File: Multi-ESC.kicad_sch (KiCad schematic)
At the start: 0 parts

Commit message: selected parts
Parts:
- added U3: LMR51450FN, Package_TO_SOT_SMD:SOT-23-6, symbol Multi-ESC:LMR51450FN
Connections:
- new net: U3.1 (SW), U3.2 (SW), U3.3 (SW)
- new net VIN: U3.10 (VIN), U3.11 (VIN), U3.12 (VIN)
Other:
- added sheet BLDC Driver (bldc_driver.kicad_sch)
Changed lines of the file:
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@@
 	(generator_version "10.0")
 	(paper "A4")
+	(symbol
+		(lib_id "Multi-ESC:LMR51450FN")
+		(at 88.9 55.88 0)
+		(unit 1)
+		(body_style 1)
+		(exclude_from_sim no)
+		(in_bom yes)
+		(on_board yes)
+		(in_pos_files yes)
+		(dnp no)
+		(fields_autoplaced yes)
+		(property "Reference" "U3"
+			(at 88.9 45.72 0)
+			(show_name no)
+			(do_not_autoplace no)
+			(effects
+				(font
+					(size 1.27 1.27)
+				)
+			)
+		)
+		(property "Value" "LMR51450FN"
+			(at 88.9 48.26 0)
+			(show_name no)
+			(do_not_autoplace no)
+			(effects
+				(font
+					(size 1.27 1.27)
+				)
+			)
+		)
+		(property "Footprint" "Package_TO_SOT_SMD:SOT-23-6"
+			(at 90.17 73.914 0)
+			(hide yes)
+			(show_name no)
+			(do_not_autoplace no)
+			(effects
+				(font
+					(size 1.27 1.27)
+				)
+				(justify left)
+			)
+		)
+		(property "Datasheet" "https://www.ti.com/lit/ds/symlink/lmr51450.pdf"
+			(at 90.17 76.454 0)
+			(hide yes)
+			(show_name no)
+			(do_not_autoplace no)
+			(effects
+				(font
+					(size 1.27 1.27)
+				)
+				(justify left)
+			)
+		)
+		(property "Description" "4.5-V to 36-V, 3-A synchronous buck converter with 40-µA IQ, SOT-23-6"
+			(at 88.9 55.88 0)
+			(hide yes)
+			(show_name no)
+			(do_not_autoplace no)
+			(effects
+				(font
+					(size 1.27 1.27)
+				)
+			)
+		)
+		(pin "12"
+		)
+		(pin "9"
+		)
+		(pin "8"
+		)
+		(pin "7"
+		)
+		(pin "1"
+		)
+		(pin "2"
+		)
+		(pin "6"
+		)
+		(pin "10"
+		)
+		(pin "11"
+		)
+		(pin "13"
+		)
+		(pin "3"
+		)
+		(pin "5"
+		)
+		(pin "4"
+		)
+		(instances
+			(project "Multi-ESC"
+				(path "/332a84c1-656a-45ff-900c-4414e0318fba"
+					(reference "U3")
+					(unit 1)
+				)
+			)
+		)
+	)
+	(sheet
+		(at 194.31 44.45)
+		(size 25.4 15.24)
+		(exclude_from_sim no)
+		(in_bom yes)
+		(on_board yes)
+		(dnp no)
+		(fields_autoplaced yes)
+		(stroke
+			(width 0.1524)
+			(type solid)
+		)
+		(fill
+			(color 0 0 0 0)
+		)
+		(property "Sheetname" "BLDC Driver"
+			(at 194.31 43.7384 0)
+			(show_name no)
+			(do_not_autoplace no)
+			(effects
+				(font
+					(size 1.27 1.27)
+				)
+				(justify left bottom)
+			)
+		)
+		(property "Sheetfile" "bldc_driver.kicad_sch"
+			(at 194.31 60.2746 0)
+			(show_name no)
+			(do_not_autoplace no)
+			(effects
+				(font
+					(size 1.27 1.27)
+				)
+				(justify left top)
+			)
+		)
+		(instances
+			(project "Multi-ESC"
+				(path "/332a84c1-656a-45ff-900c-4414e0318fba"
+					(page "2")
+				)
+			)
+		)
+	)
 	(sheet_instances
 		(path "/"

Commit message: wired regulator
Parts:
- added C1, C2, C3, C4: 100nF, symbol Device:C
- added C5, C6, C7: 10uF, symbol Device:C
- added L1: 4.7uH, symbol Device:L
- added R1, R4: 100K, symbol Device:R
- added R2: 32K, symbol Device:R
- added R3: 30.9K, symbol Device:R
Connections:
- net VIN is gone; now on net VBUS: U3.10 (VIN), U3.11 (VIN), U3.12 (VIN)
- net at U3.1 (SW), U3.2 (SW), U3.3 (SW): now also C1.2, L1.1
- net GND: now reaches U3.13 (GND)
- net GND: now also U3.8 (AGND), C2.2, C3.2, C4.2, C5.2, C6.2, C7.2, R2.2, R3.2
- net at U3.4 (BOOT): now also C1.1
- net at U3.5 (PG): now also R4.1
- net at U3.6 (RT): now also R3.1
- net at U3.7 (FB): now also R1.2, R2.1
- net VBUS: now reaches U3.9 (EN)
- net VBUS: now also C4.1, C5.1, C6.1, C7.1
- new net +3.3V: C2.1, C3.1, L1.2, R1.1, R4.2
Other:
- moved on the sheet: U3

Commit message: started driver circuit
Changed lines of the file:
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@@
 	)
 	(sheet
-		(at 194.31 44.45)
-		(size 25.4 15.24)
+		(at 167.64 42.545)
+		(size 42.545 34.925)
 		(exclude_from_sim no)
 		(in_bom yes)
@@
 		)
 		(property "Sheetname" "BLDC Driver"
-			(at 194.31 43.7384 0)
+			(at 167.64 41.8334 0)
 			(show_name no)
 			(do_not_autoplace no)
@@
 		)
 		(property "Sheetfile" "bldc_driver.kicad_sch"
-			(at 194.31 60.2746 0)
+			(at 167.64 78.0546 0)
 			(show_name no)
 			(do_not_autoplace no)

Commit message: wired mcu circuit
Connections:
- net GND: no longer U3.8 (AGND)
- new net GNDA: U3.8 (AGND)
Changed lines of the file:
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@@
 	)
 	(symbol
-		(lib_id "power:GND")
+		(lib_id "power:GNDA")
 		(at 102.87 179.07 0)
 		(unit 1)
@@
 		(in_pos_files yes)
 		(dnp no)
-		(property "Reference" "#PWR02"
+		(property "Reference" "#PWR020"
 			(at 102.87 185.42 0)
 			(hide yes)
@@
 			)
 		)
-		(property "Value" "GND"
-			(at 102.87 182.88 0)
+		(property "Value" "GNDA"
+			(at 102.87 183.134 0)
 			(show_name no)
 			(do_not_autoplace no)
@@
 			)
 		)
-		(property "Description" "Power symbol creates a global label with name \"GND\" , ground"
+		(property "Description" "Power symbol creates a global label with name \"GNDA\" , analog ground"
 			(at 102.87 179.07 0)
 			(hide yes)
@@
 			(project "Multi-ESC"
 				(path "/332a84c1-656a-45ff-900c-4414e0318fba"
-					(reference "#PWR02")
+					(reference "#PWR020")
 					(unit 1)
 				)

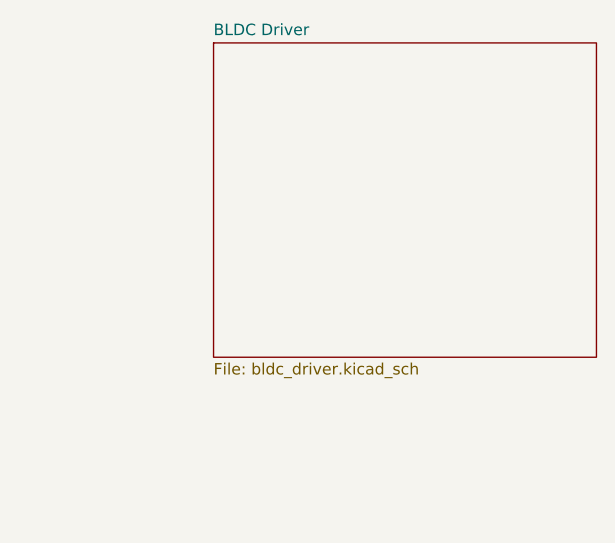
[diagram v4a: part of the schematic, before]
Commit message: started wiring gate driver
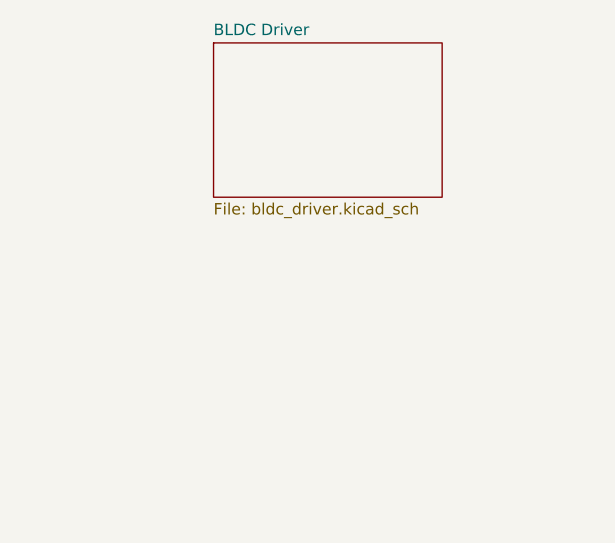
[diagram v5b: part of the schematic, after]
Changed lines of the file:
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@@
 	(sheet
 		(at 167.64 42.545)
-		(size 42.545 34.925)
+		(size 25.4 17.145)
 		(exclude_from_sim no)
 		(in_bom yes)
@@
 		)
 		(property "Sheetfile" "bldc_driver.kicad_sch"
-			(at 167.64 78.0546 0)
+			(at 167.64 60.2746 0)
 			(show_name no)
 			(do_not_autoplace no)

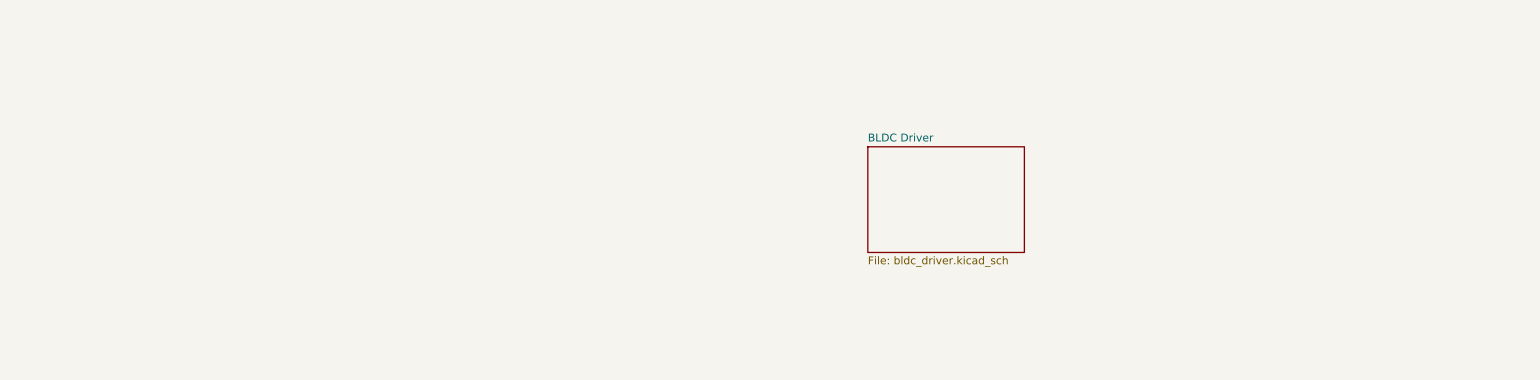
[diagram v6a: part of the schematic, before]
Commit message: added bulk capacitance
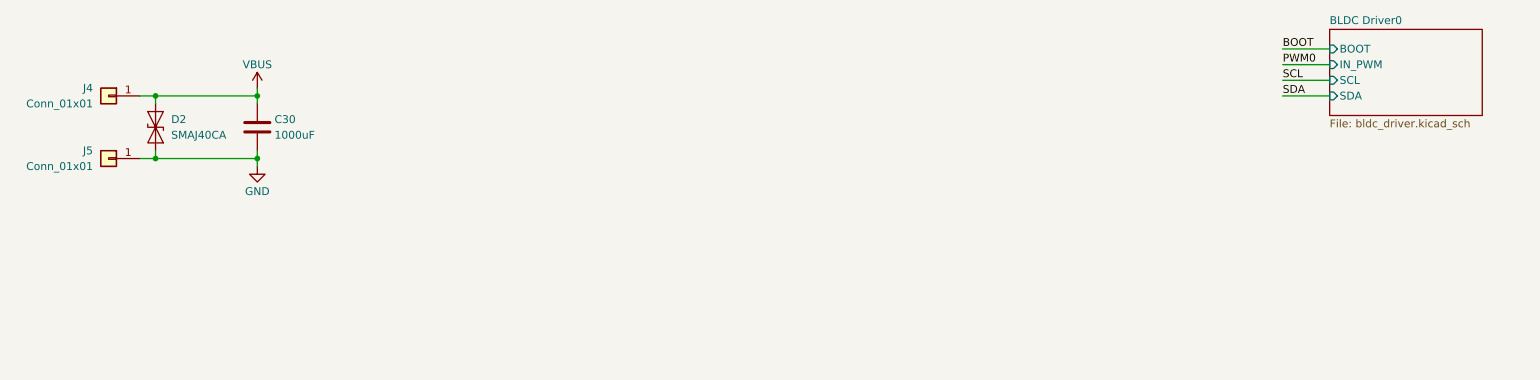
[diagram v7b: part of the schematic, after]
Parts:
- added C30: 1000uF, symbol Device:C
- added D2: SMAJ40CA, Diode_SMD:D_SMA, symbol Diode:SMAJ40CA
- added J4, J5: Conn_01x01, symbol Connector_Generic:Conn_01x01
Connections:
- net GND: now also C30.2, D2.1 (A1), J5.1 (Pin_1)
- net VBUS: now also C30.1, D2.2 (A2), J4.1 (Pin_1)
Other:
- sheet BLDC Driver renamed BLDC Driver0
- sheet BLDC Driver0 ports: added BOOT, IN_PWM, SCL, SDA; removed none

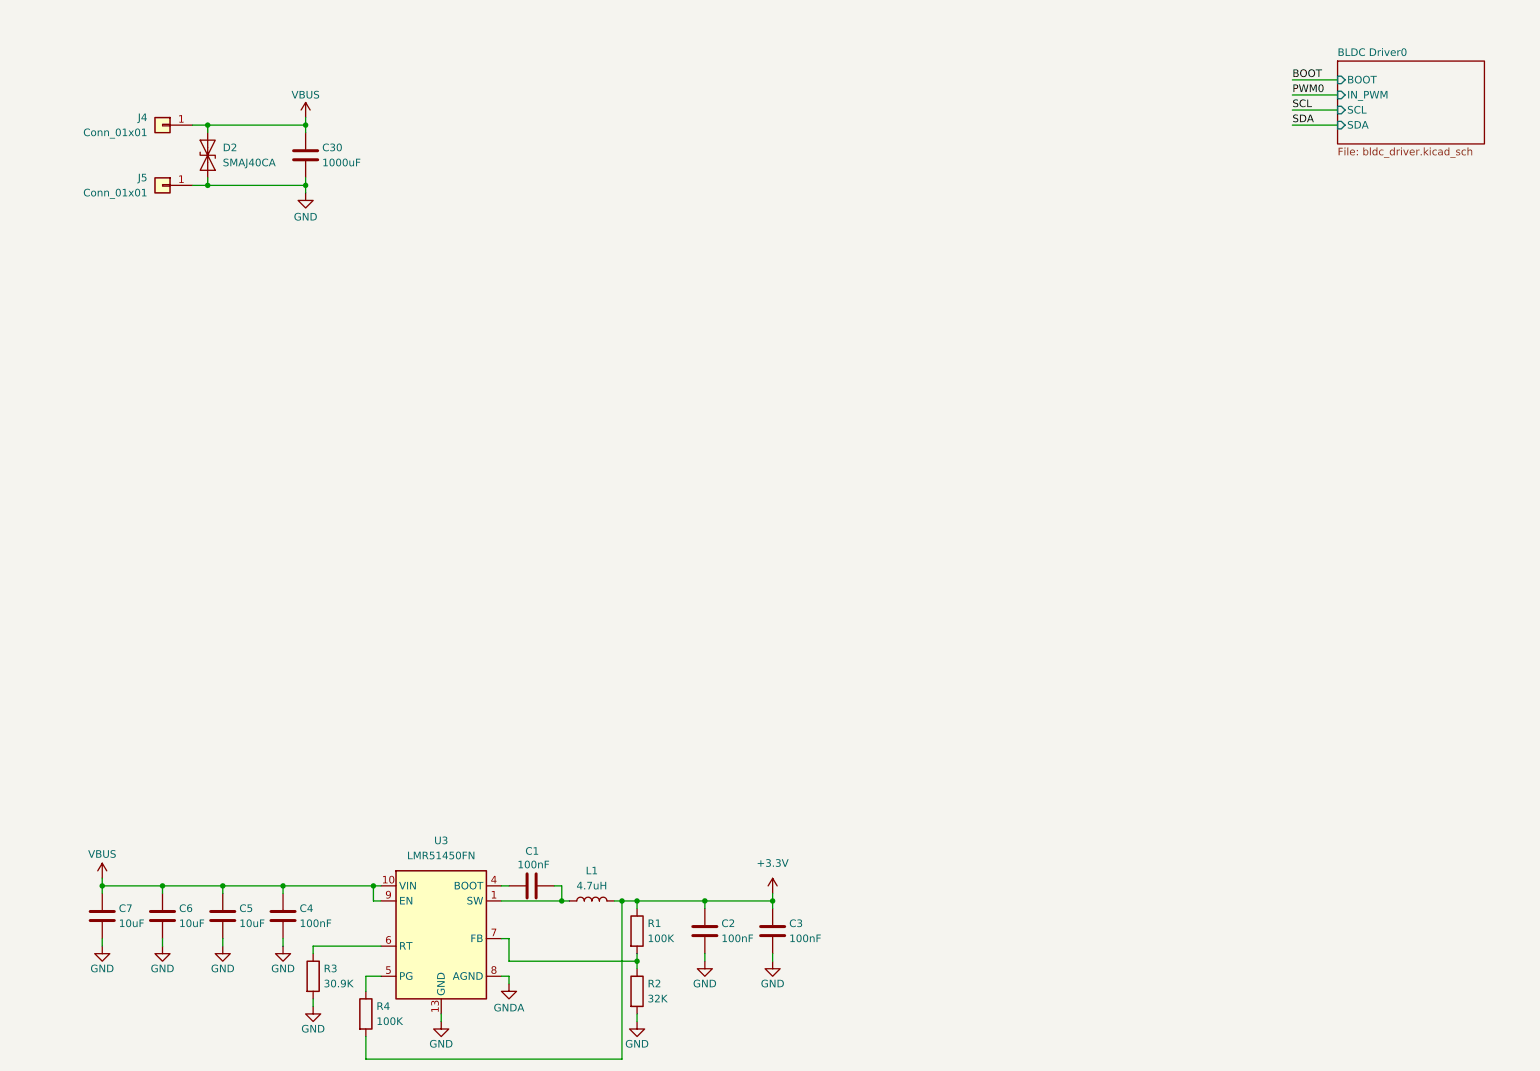
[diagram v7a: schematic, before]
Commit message: started pcb layout
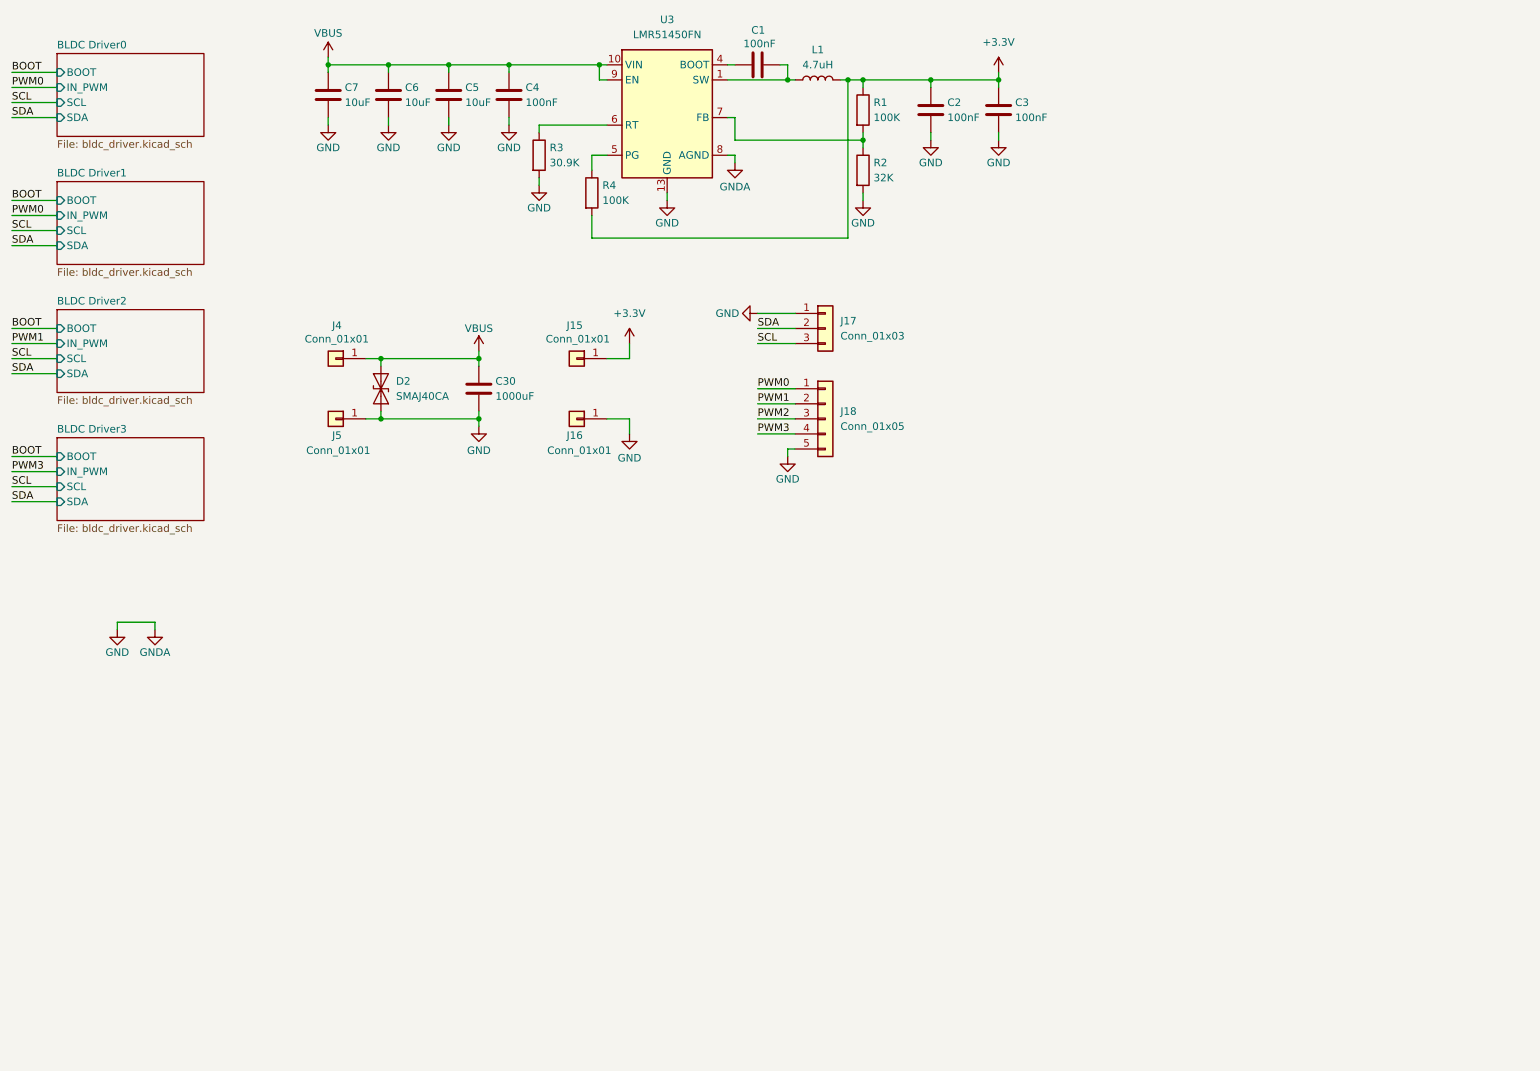
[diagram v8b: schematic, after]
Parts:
- added J15, J16: Conn_01x01, Connector_Wire:SolderWire-2sqmm_1x01_D2mm_OD3.9mm, symbol Connector_Generic:Conn_01x01
- added J17: Conn_01x03, Connector_PinSocket_2.54mm:PinSocket_1x03_P2.54mm_Vertical, symbol Connector_Generic:Conn_01x03
- added J18: Conn_01x05, Connector_PinSocket_2.54mm:PinSocket_1x05_P2.54mm_Vertical, symbol Connector_Generic:Conn_01x05
- C1, C2, C3, C4: footprint (none) -> Capacitor_SMD:C_0402_1005Metric
- C5, C6, C7: footprint (none) -> Capacitor_SMD:C_0603_1608Metric
- J4, J5: footprint (none) -> Connector_Wire:SolderWire-4sqmm_1x01_D3mm_OD6mm
- L1: footprint (none) -> Inductor_SMD:L_Pulse_PA4320
- R1, R2, R3, R4: footprint (none) -> Resistor_SMD:R_0402_1005Metric
- U3: footprint Package_TO_SOT_SMD:SOT-23-6 -> Package_SON:WSON-12-1EP_3x3mm_P0.5mm_EP1.5x2.5mm_ThermalVias
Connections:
- net GNDA is gone; now on net GND: U3.8 (AGND)
- net +3.3V: now also J15.1 (Pin_1)
- net GND: now also J16.1 (Pin_1), J17.1 (Pin_1), J18.5 (Pin_5)
- net PWM0: now also J18.1 (Pin_1)
- net SCL: now also J17.3 (Pin_3)
- net SDA: now also J17.2 (Pin_2)
- new net PWM1: J18.2 (Pin_2)
- new net PWM2: J18.3 (Pin_3)
- new net PWM3: J18.4 (Pin_4)
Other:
- added sheet BLDC Driver1 (bldc_driver.kicad_sch)
- added sheet BLDC Driver2 (bldc_driver.kicad_sch)
- added sheet BLDC Driver3 (bldc_driver.kicad_sch)
- moved on the sheet: C1, C2, C3, C30, C4, C5, C6, C7, D2, J4, J5, L1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
